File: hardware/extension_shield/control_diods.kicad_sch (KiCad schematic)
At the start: 16 parts, among them J5 Conn_02x05_Odd_Even, Q1 BC546, Q2 BC546, Q3 BC546, Q4 BC546, Q5 BC546

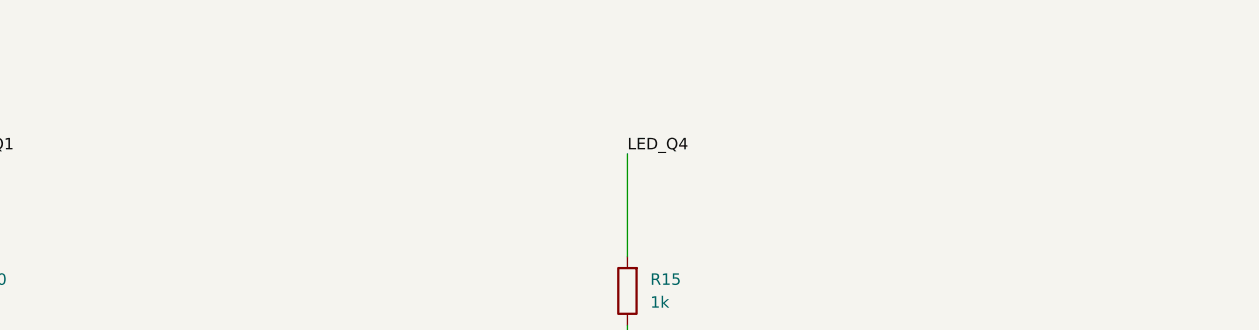
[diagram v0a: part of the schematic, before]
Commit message: [HW] Adds Labels To Expansion Shield Schematic, PDF Schematic & Performed Schematic, PCB Tests.
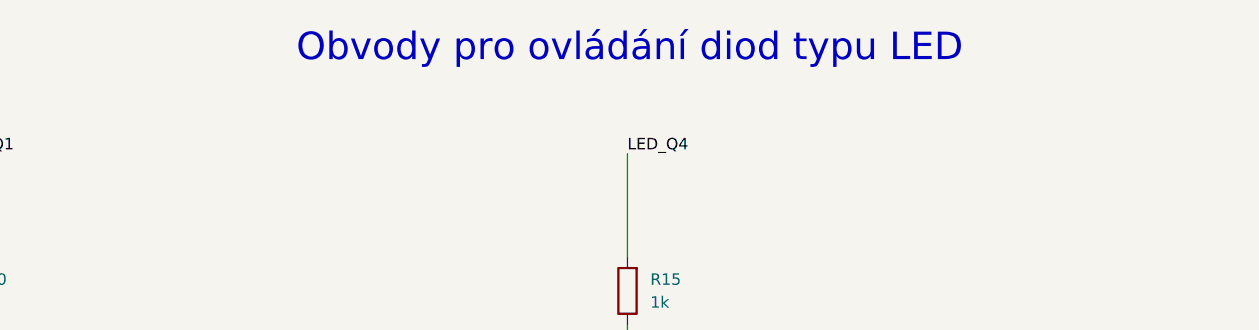
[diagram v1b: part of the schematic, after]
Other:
- note added: "Obvody pro ovládání diod typu LED"
- title: Datalogger Expansion Shield -> Data Logger Expansion Shield
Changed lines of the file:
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@@
 	(paper "A4")
 	(title_block
-		(title "Datalogger Expansion Shield")
+		(title "Data Logger Expansion Shield")
 		(date "2025-02-26")
 		(rev "1.2")
@@
 		)
 	)
+	(text "Obvody pro ovládání diod typu LED"
+		(exclude_from_sim no)
+		(at 157.734 26.416 0)
+		(effects
+			(font
+				(size 3.048 3.048)
+			)
+		)
+	)
